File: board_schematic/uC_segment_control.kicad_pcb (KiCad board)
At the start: 2 copper layers, 69.9 x 41.9 mm, 14 parts, among them P1 CONN_02X05, P2 POWER_IN, U1 LF33

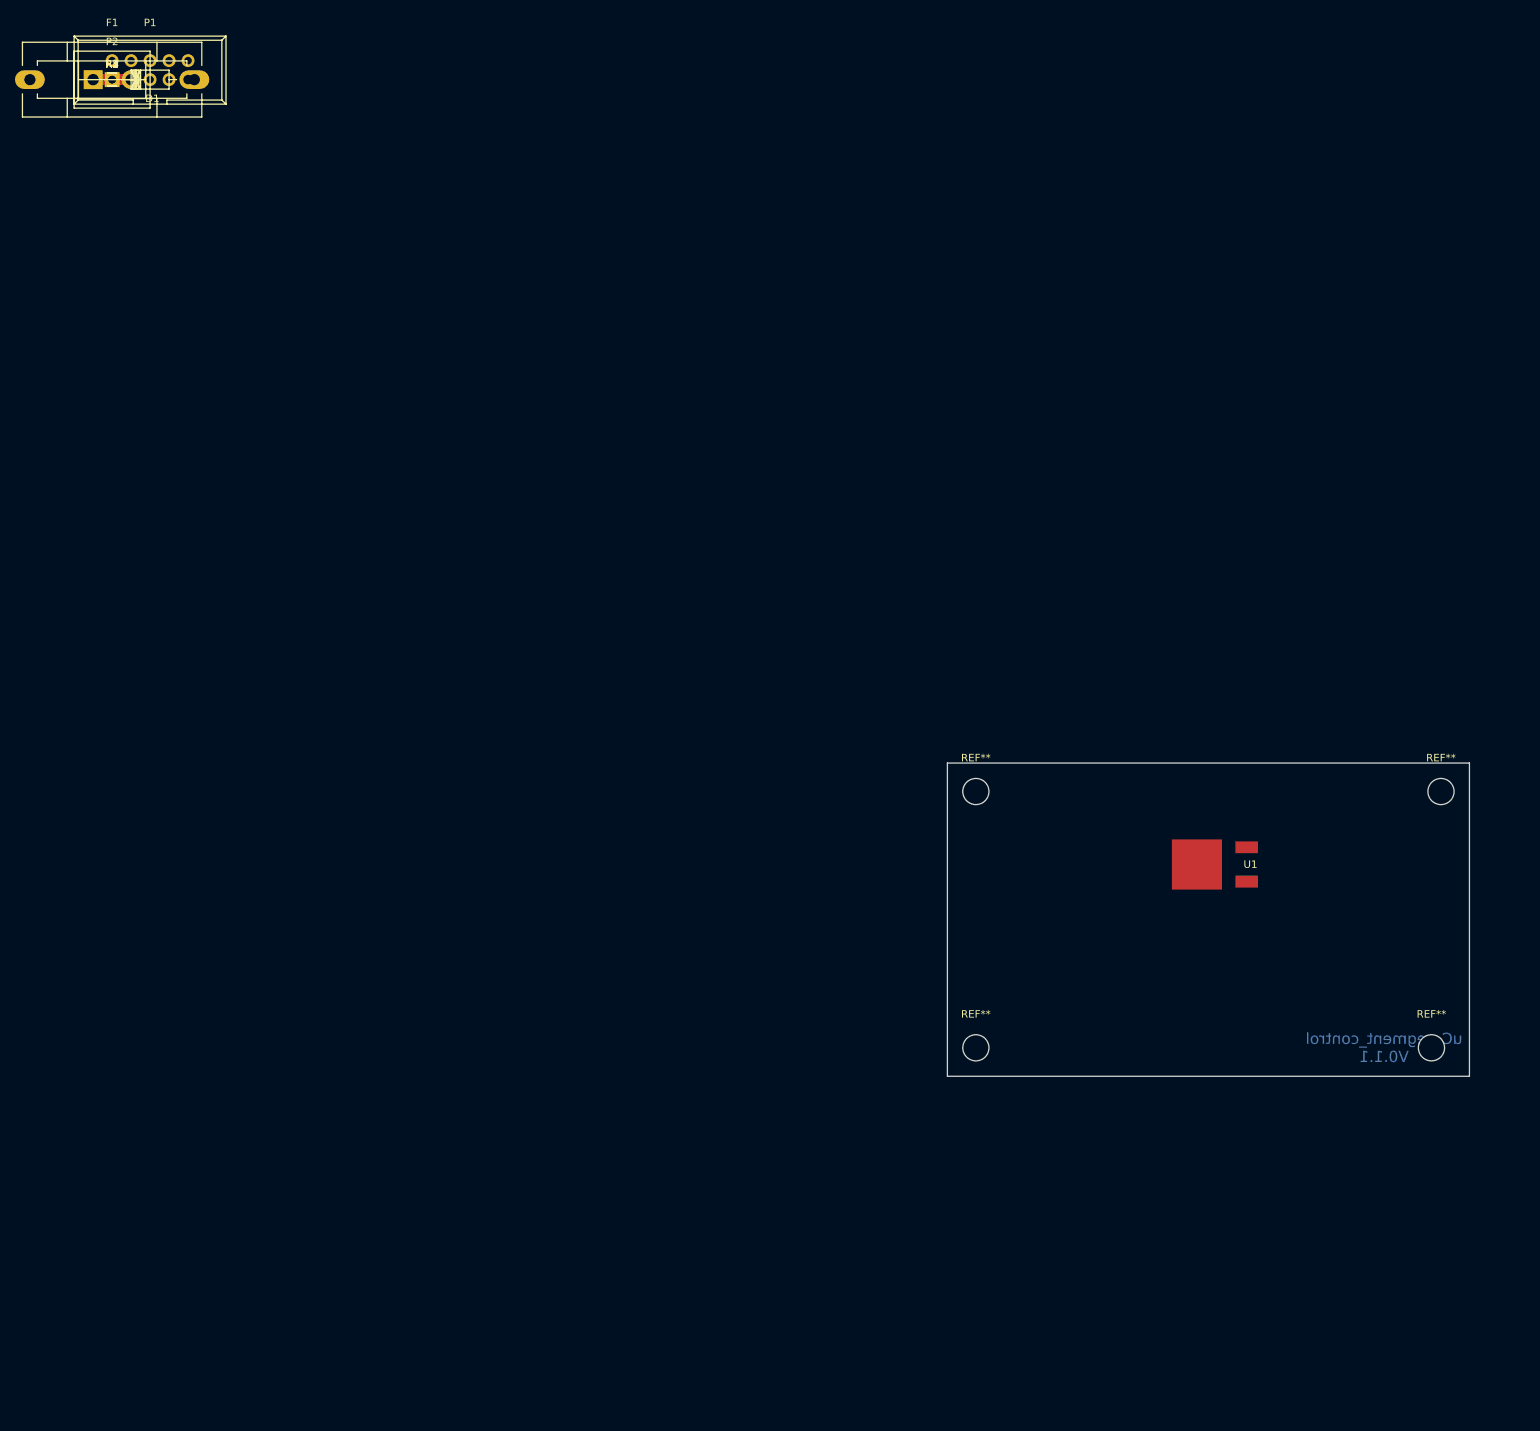
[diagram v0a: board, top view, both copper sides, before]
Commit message: V0.2.1: First schematic for BOM
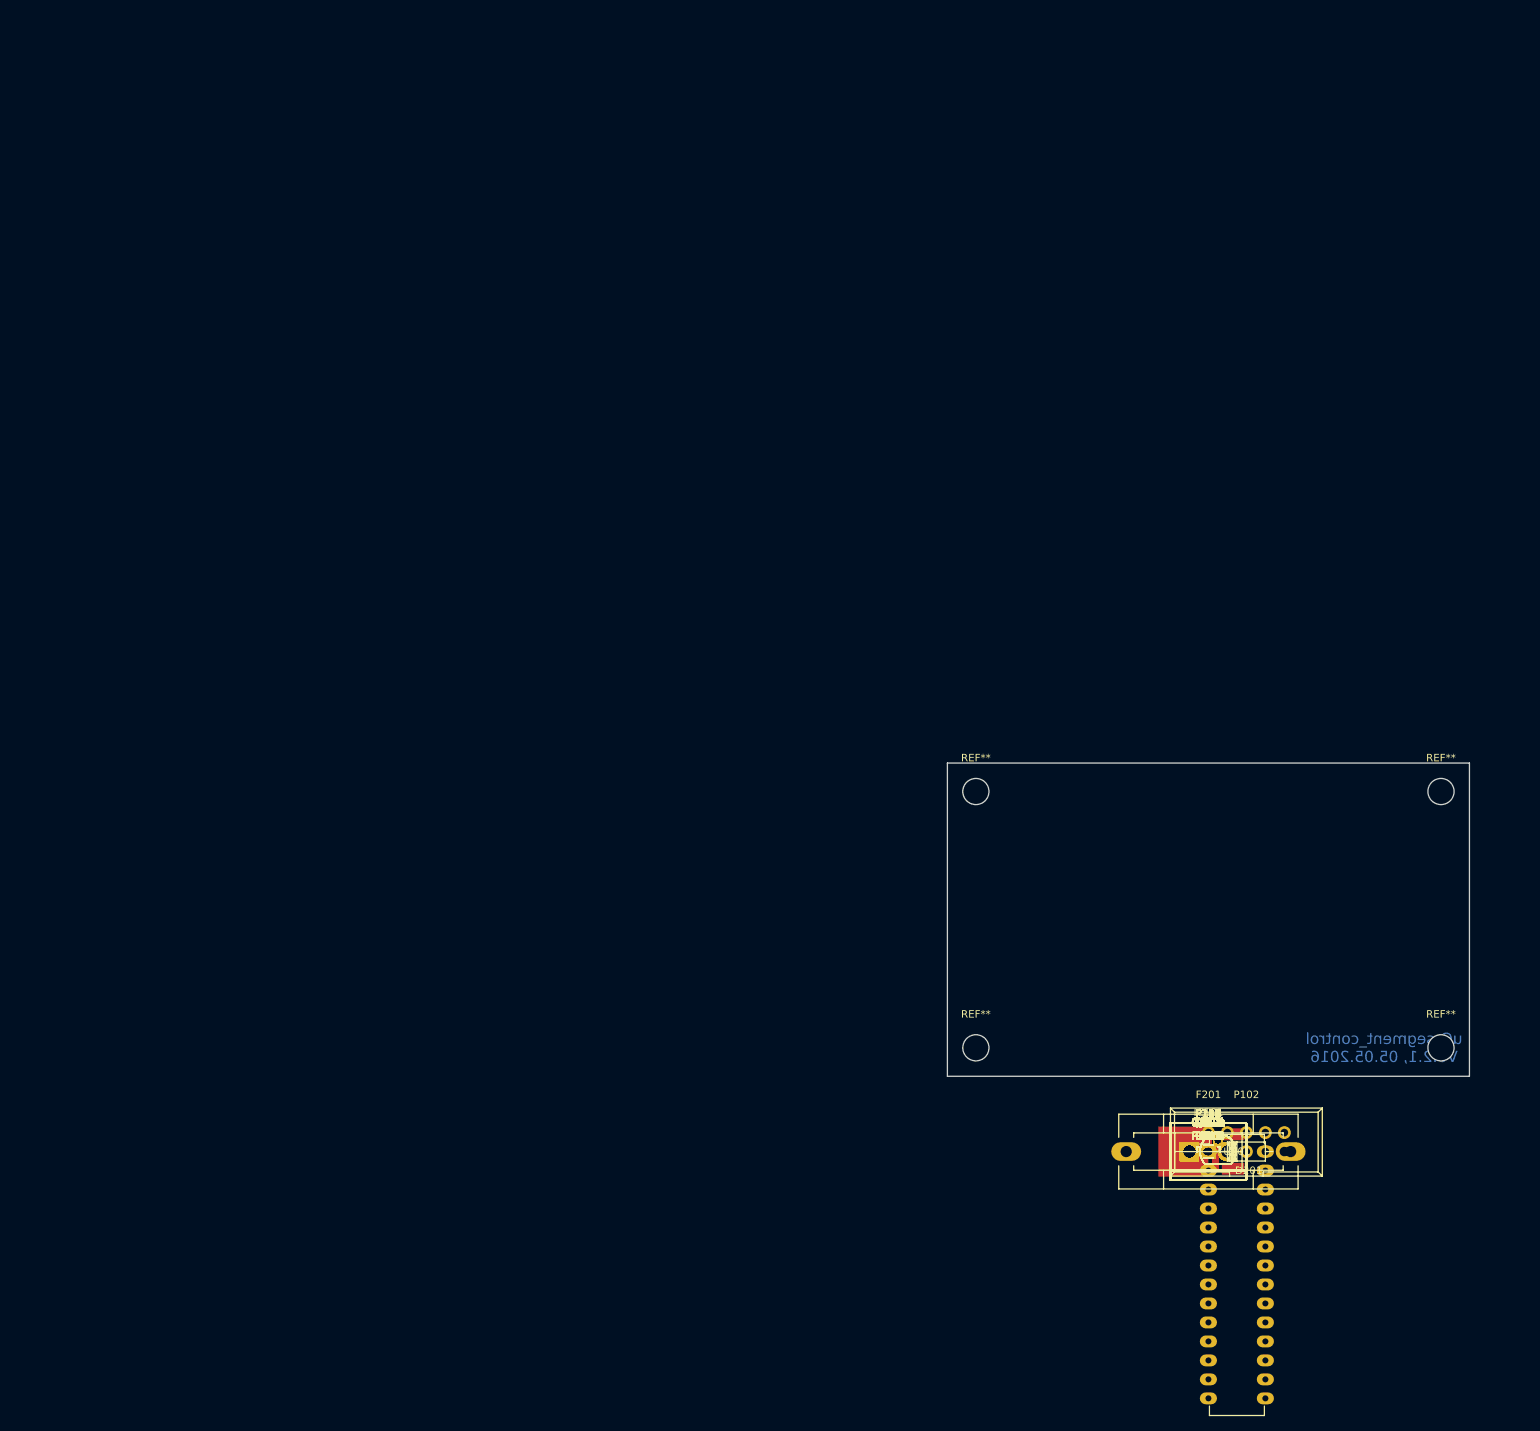
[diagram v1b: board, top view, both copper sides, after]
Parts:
- removed D1: ZD 15, Diodes_ThroughHole:Diode_DO-41_SOD81_Horizontal_RM10
- removed F1: 2.5A, Fuse_Holders_and_Fuses:Fuseholder5x20_horiz_SemiClosed_Casing10x25mm
- removed P1: CONN_02X05, Connect:IDC_Header_Straight_10pins
- removed P2: POWER_IN, Connect:bornier2
- removed R1, R2, R3, R4: 5k, Resistors_SMD:R_0805_HandSoldering
- removed R5: 10k, Resistors_SMD:R_0805_HandSoldering
- removed U1: LF33, project_footprints:D-PAK
- added C101: C, Capacitors_SMD:C_0805_HandSoldering, F.Cu at (146.7, 143.4)
- added C102: C_Small, Capacitors_SMD:C_0805_HandSoldering, F.Cu at (146.7, 143.4)
- added C201: 1uF (X7R-G0805 1,0/25), Capacitors_SMD:C_0805_HandSoldering, F.Cu at (146.7, 143.4)
- added C202: 10uF (X5R-G0805 10/16), Capacitors_SMD:C_0805_HandSoldering, F.Cu at (146.7, 143.4)
- added D201: ZD 15, Diodes_ThroughHole:Diode_DO-41_SOD81_Horizontal_RM10, F.Cu at (146.7, 143.4)
- added F201: F_Power, Fuse_Holders_and_Fuses:Fuseholder5x20_horiz_SemiClosed_Casing10x25mm, F.Cu at (146.7, 143.4)
- added IC101: ATMEGA88PA-P, Housings_DIP:DIP-28_W7.62mm_LongPads, F.Cu at (146.7, 143.4)
- added P101, P103, P104, P105, P106, P107, P108, P109, P110, P111, P112, P113, P114, P115, P116, P117, P118, P119, P120, P121, P122, P123, P124, P125, P126, P127, P128, P129, P130, P131, P132, P133, P134: CONN_01X02, Connect:bornier2, F.Cu at (146.7, 143.4)
- added P102: CONN_02X05, Connect:IDC_Header_Straight_10pins, F.Cu at (146.7, 143.4)
- added P201: CONN_01X02_P, Connect:bornier2, F.Cu at (146.7, 143.4)
- added Q1001, Q1101, Q1201, Q1301, Q1401, Q1501, Q1601, Q301, Q401, Q501, Q601, Q701, Q801, Q901: BC548, project_footprints:TO-92_Molded_0.6space_Oval, F.Cu at (146.7, 143.4)
- added Q1002, Q1102, Q1202, Q1302, Q1402, Q1502, Q1602, Q302, Q402, Q502, Q602, Q702, Q802, Q902: IRLML2244, TO_SOT_Packages_SMD:SOT-23_Handsoldering, F.Cu at (146.7, 143.4)
- added Q101, Q102, Q103, Q104, Q105, Q106: IRLML2502, TO_SOT_Packages_SMD:SOT-23_Handsoldering, F.Cu at (146.7, 143.4)
- added R1001, R1101, R1201, R1301, R1401, R1501, R1601, R301, R401, R501, R601, R701, R801, R901: 5k4, Resistors_SMD:R_0805_HandSoldering, F.Cu at (146.7, 143.4)
- added R1002, R1102, R1202, R1302, R1402, R1502, R1602, R302, R402, R502, R602, R702, R802, R902: 2k5, Resistors_SMD:R_0805_HandSoldering, F.Cu at (146.7, 143.4)
- added R1003, R1103, R1203, R1303, R1403, R1503, R1603, R303, R403, R503, R603, R703, R803, R903: 24k, Resistors_SMD:R_0805_HandSoldering, F.Cu at (146.7, 143.4)
- added R101, R102: 100, Resistors_SMD:R_0805_HandSoldering, F.Cu at (146.7, 143.4)
- added R103, R104, R105, R106: 5k, Resistors_SMD:R_0805_HandSoldering, F.Cu at (146.7, 143.4)
- added R107, R108, R109, R110, R111, R112: 250, Resistors_SMD:R_0805_HandSoldering, F.Cu at (146.7, 143.4)
- added R113: 10k, Resistors_SMD:R_0805_HandSoldering, F.Cu at (146.7, 143.4)
- added R114, R115, R116, R117, R118, R119: 3k3, Resistors_SMD:R_0805_HandSoldering, F.Cu at (146.7, 143.4)
- added U201: LF33, project_footprints:D-PAK, F.Cu at (146.7, 143.4)
- moved REF** 1.27 mm to (177.8, 129.5)
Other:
- net class Default: clearance 0.2 -> 0.6; trace_width 0.25 -> 1; via_dia 0.6 -> 1.5; via_drill 0.4 -> 0.8
- rule trace_clearance: 0.2 -> 0.6
- rule via_min_drill: 0.3 -> 0.8
- rule via_min_size: 0.4 -> 1.4
- board text added: "uC_segment_control V0.2.1, 05.05.2016"
- board text removed: "uC_segment_control V0.1.1"

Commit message: V0.3.1: First layout
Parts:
- removed P131, P132, P133, P134: CONN_01X02, Connect:bornier2
- removed the REF** at (115.6, 129.5)
- removed the REF** at (115.6, 95.2)
- removed the REF** at (177.8, 95.2)
- removed the REF** at (177.8, 129.5)
- added R120: 100, Resistors_SMD:R_0805_HandSoldering, B.Cu at (102.2, 126.8)
- added R121: 100, Resistors_SMD:R_0805_HandSoldering, B.Cu at (107.2, 126.8)
- added REF**: MountingHole_3mm, Mounting_Holes:MountingHole_3mm, F.Cu at (54.0, 140.0)
- added REF**: MountingHole_3mm, Mounting_Holes:MountingHole_3mm, F.Cu at (185.0, 140.0)
- added REF**: MountingHole_3mm, Mounting_Holes:MountingHole_3mm, F.Cu at (185.0, 54.0)
- added REF**: MountingHole_3mm, Mounting_Holes:MountingHole_3mm, F.Cu at (54.0, 54.0)
- C101: value C -> 100n; moved to B.Cu
- C102: value C_Small -> 100n; moved to B.Cu
- C201, C202, Q101, Q102, Q103, Q104, Q105, Q106, R116, R117, R118, U201: moved to B.Cu
- P101, P103, P104, P105, P106, P121, P122: value CONN_01X02 -> CONN_01X03; footprint Connect:bornier2 -> Connect:AK300-3
- P102: value CONN_02X05 -> CONN_01X03; footprint Connect:IDC_Header_Straight_10pins -> Connect:AK300-3
- P107, P108, P109, P110, P111, P112, P113, P114, P115, P116, P117, P118, P119, P120, P123, P124, P125, P126, P127, P129, P130, P201: footprint Connect:bornier2 -> Connect:AK300-2
- P128: value CONN_01X02 -> CONN_02X05; footprint Connect:bornier2 -> Connect:IDC_Header_Straight_10pins
- Q1001, Q1101, Q1201, Q1301, Q1401, Q1501, Q1601, Q301, Q401, Q501, Q601, Q701, Q801, Q901: value BC548 -> IRLML2244; footprint project_footprints:TO-92_Molded_0.6space_Oval -> TO_SOT_Packages_SMD:SOT-23_Handsoldering; moved to B.Cu
- Q1002, Q1102, Q1202, Q1302, Q1402, Q1502, Q1602, Q302, Q402, Q502, Q602, Q702, Q802, Q902: value IRLML2244 -> BC548; footprint TO_SOT_Packages_SMD:SOT-23_Handsoldering -> project_footprints:TO-92_Molded_0.6space_Oval
- R1001, R1101, R1201, R1301, R1401, R1501, R1601, R301, R401, R501, R601, R701, R801, R901: value 5k4 -> 27k; moved to B.Cu
- R1002, R1102, R1202, R1302, R1402, R1502, R1602, R302, R402, R502, R602, R702, R802, R902: value 2k5 -> 5k6; moved to B.Cu
- R1003, R1103, R1203, R1303, R1403, R1503, R1603, R303, R403, R503, R603, R703, R803, R903: value 24k -> 2k7; moved to B.Cu
- R101, R102: value 100 -> 270; moved to B.Cu
- R103: value 5k -> 270; moved to B.Cu
- R104, R105, R106: value 5k -> 3k3; moved to B.Cu
- R107: value 250 -> 10k; moved to B.Cu
- R108, R109, R110: value 250 -> 270; moved to B.Cu
- R111, R112: value 250 -> 5k; moved to B.Cu
- R113: value 10k -> 5k; moved to B.Cu
- R114, R115, R119: value 3k3 -> 5k; moved to B.Cu
- moved R302 119.1 mm to (55.2, 67.2)
- moved R303 116.7 mm to (55.2, 71.0)
- moved R402 115.3 mm to (60.2, 67.2)
- moved Q302 113.5 mm to (55.9, 75.2), turned to 90 degrees
- moved R403 112.8 mm to (60.2, 71.0)
- moved R502 111.6 mm to (65.2, 67.2)
- moved Q402 109.6 mm to (60.9, 75.2), turned to 90 degrees
- moved P119 109.3 mm to (55.5, 83.2)
- moved R503 109.1 mm to (65.2, 71.0)
- moved R602 108.0 mm to (70.2, 67.2)
- moved Q301 107.0 mm to (55.5, 87.5), turned to 180 degrees
- moved Q502 105.7 mm to (65.9, 75.2), turned to 90 degrees
- moved R603 105.4 mm to (70.2, 71.0)
- moved R301 105.4 mm to (55.5, 90.7)
- moved R702 104.5 mm to (75.2, 67.2)
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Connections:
- IC101 pad 21: (no net) -> Net-(IC101-Pad21)
- P101 pad 2: Net-(P101-Pad2) -> Net-(P101-Pad1)
- P102 pad 1: Net-(P102-Pad1) -> Net-(P101-Pad1)
- P102 pad 2: (no net) -> Net-(P101-Pad1)
- P102 pad 3: (no net) -> Net-(P101-Pad1)
- P103 pad 1: /p-mos_switch_S0_0.sch/S_OUT -> Net-(P103-Pad1)
- P103 pad 2: /p-mos_switch_S0_1.sch/S_OUT -> Net-(P103-Pad1)
- P104 pad 1: /p-mos_switch_S0_2.sch/S_OUT -> Net-(P103-Pad1)
- P104 pad 2: /p-mos_switch_S0_3.sch/S_OUT -> Net-(P103-Pad1)
- P105 pad 1: /p-mos_switch_S0_4.sch/S_OUT -> Net-(P105-Pad1)
- P105 pad 2: /p-mos_switch_S0_5.sch/S_OUT -> Net-(P105-Pad1)
- P106 pad 1: /p-mos_switch_S0_6.sch/S_OUT -> Net-(P105-Pad1)
- P106 pad 2: /p-mos_switch_S1_0.sch/S_OUT -> Net-(P105-Pad1)
- P107 pad 1: /p-mos_switch_S1_1.sch/S_OUT -> Net-(P101-Pad1)
- P107 pad 2: /p-mos_switch_S1_2.sch/S_OUT -> Net-(P101-Pad1)
- P108 pad 1: /p-mos_switch_S1_3.sch/S_OUT -> Net-(P101-Pad1)
- P108 pad 2: /p-mos_switch_S1_4.sch/S_OUT -> Net-(P101-Pad1)
- P109 pad 1: /p-mos_switch_S1_5.sch/S_OUT -> Net-(P103-Pad1)
- P109 pad 2: /p-mos_switch_S1_6.sch/S_OUT -> Net-(P103-Pad1)
- P110 pad 1: +12.0V -> Net-(P103-Pad1)
- P110 pad 2: +12.0V -> Net-(P103-Pad1)
- P111 pad 1: Net-(P111-Pad1) -> Net-(P105-Pad1)
- P111 pad 2: Net-(P111-Pad1) -> Net-(P105-Pad1)
- P112 pad 1: Net-(P111-Pad1) -> Net-(P105-Pad1)
- P112 pad 2: Net-(P111-Pad1) -> Net-(P105-Pad1)
- P113 pad 1: Net-(P111-Pad1) -> Net-(P101-Pad1)
- P113 pad 2: Net-(P111-Pad1) -> Net-(P101-Pad1)
- P114 pad 1: Net-(P111-Pad1) -> Net-(P101-Pad1)
- P114 pad 2: Net-(P111-Pad1) -> Net-(P101-Pad1)
- P115 pad 1: Net-(P115-Pad1) -> Net-(P103-Pad1)
- P115 pad 2: Net-(P115-Pad1) -> Net-(P103-Pad1)
- P116 pad 1: Net-(P111-Pad1) -> Net-(P103-Pad1)
- P116 pad 2: Net-(P111-Pad1) -> Net-(P103-Pad1)
- P117 pad 1: Net-(P111-Pad1) -> Net-(P105-Pad1)
- P117 pad 2: Net-(P111-Pad1) -> Net-(P105-Pad1)
- P118 pad 1: Net-(P111-Pad1) -> Net-(P105-Pad1)
- P118 pad 2: Net-(P111-Pad1) -> Net-(P105-Pad1)
- P119 pad 1: Net-(P119-Pad1) -> /p-mos_switch_S0_0.sch/S_OUT
- P119 pad 2: Net-(P119-Pad1) -> /p-mos_switch_S0_1.sch/S_OUT
- P120 pad 1: Net-(P119-Pad1) -> /p-mos_switch_S0_2.sch/S_OUT
- P120 pad 2: Net-(P119-Pad1) -> /p-mos_switch_S0_3.sch/S_OUT
- P121 pad 1: Net-(P119-Pad1) -> /p-mos_switch_S0_4.sch/S_OUT
- P121 pad 2: Net-(P119-Pad1) -> /p-mos_switch_S0_5.sch/S_OUT
- P122 pad 1: Net-(P119-Pad1) -> /p-mos_switch_S1_0.sch/S_OUT
- P122 pad 2: Net-(P119-Pad1) -> /p-mos_switch_S1_1.sch/S_OUT
- P123 pad 1: Net-(P123-Pad1) -> /p-mos_switch_S1_3.sch/S_OUT
- P123 pad 2: Net-(P123-Pad1) -> /p-mos_switch_S1_4.sch/S_OUT
- P124 pad 1: Net-(P119-Pad1) -> /p-mos_switch_S1_5.sch/S_OUT
- P124 pad 2: Net-(P119-Pad1) -> /p-mos_switch_S1_6.sch/S_OUT
- P125 pad 1: Net-(P119-Pad1) -> Net-(P125-Pad1)
- P125 pad 2: Net-(P119-Pad1) -> Net-(P125-Pad1)
- P126 pad 1: Net-(P119-Pad1) -> Net-(P126-Pad1)
- P126 pad 2: Net-(P119-Pad1) -> Net-(P126-Pad1)
- P128 pad 1: Net-(P127-Pad1) -> Net-(P128-Pad1)
- P128 pad 2: Net-(P127-Pad1) -> Net-(P128-Pad2)
- P129 pad 1: Net-(P127-Pad1) -> +12.0V
- P129 pad 2: Net-(P127-Pad1) -> +12.0V
- P130 pad 1: Net-(P127-Pad1) -> Net-(P130-Pad1)
- P130 pad 2: Net-(P127-Pad1) -> Net-(P130-Pad2)
- Q1001 pad 2: Net-(Q1001-Pad2) -> +12.0V
- Q1001 pad 3: GND -> /p-mos_switch_S1_0.sch/S_OUT
- Q1002 pad 2: +12.0V -> Net-(Q1002-Pad2)
- Q1002 pad 3: /p-mos_switch_S1_0.sch/S_OUT -> GND
- Q101 pad 3: Net-(P111-Pad1) -> Net-(P101-Pad1)
- Q102 pad 1: /G1_R -> /G0_G
- Q102 pad 3: Net-(P115-Pad1) -> Net-(P103-Pad1)
- Q103 pad 1: /G0_G -> /G0_B
- Q103 pad 3: Net-(P119-Pad1) -> Net-(P105-Pad1)
- Q104 pad 1: /G1_G -> /G1_R
- Q104 pad 3: Net-(P123-Pad1) -> Net-(P125-Pad1)
- Q105 pad 1: /G0_B -> /G1_G
- Q105 pad 3: Net-(P127-Pad1) -> Net-(P126-Pad1)
- Q106 pad 3: Net-(P131-Pad1) -> Net-(P127-Pad1)
- Q1101 pad 2: Net-(Q1101-Pad2) -> +12.0V
- Q1101 pad 3: GND -> /p-mos_switch_S1_1.sch/S_OUT
- Q1102 pad 2: +12.0V -> Net-(Q1102-Pad2)
- Q1102 pad 3: /p-mos_switch_S1_1.sch/S_OUT -> GND
- Q1201 pad 2: Net-(Q1201-Pad2) -> +12.0V
- Q1201 pad 3: GND -> /p-mos_switch_S1_2.sch/S_OUT
- Q1202 pad 2: +12.0V -> Net-(Q1202-Pad2)
- Q1202 pad 3: /p-mos_switch_S1_2.sch/S_OUT -> GND
- Q1301 pad 2: Net-(Q1301-Pad2) -> +12.0V
- Q1301 pad 3: GND -> /p-mos_switch_S1_3.sch/S_OUT
- Q1302 pad 2: +12.0V -> Net-(Q1302-Pad2)
- Q1302 pad 3: /p-mos_switch_S1_3.sch/S_OUT -> GND
- Q1401 pad 2: Net-(Q1401-Pad2) -> +12.0V
- Q1401 pad 3: GND -> /p-mos_switch_S1_4.sch/S_OUT
- Q1402 pad 2: +12.0V -> Net-(Q1402-Pad2)
- Q1402 pad 3: /p-mos_switch_S1_4.sch/S_OUT -> GND
- Q1501 pad 2: Net-(Q1501-Pad2) -> +12.0V
- Q1501 pad 3: GND -> /p-mos_switch_S1_5.sch/S_OUT
- Q1502 pad 2: +12.0V -> Net-(Q1502-Pad2)
- Q1502 pad 3: /p-mos_switch_S1_5.sch/S_OUT -> GND
- Q1601 pad 2: Net-(Q1601-Pad2) -> +12.0V
- Q1601 pad 3: GND -> /p-mos_switch_S1_6.sch/S_OUT
- Q1602 pad 2: +12.0V -> Net-(Q1602-Pad2)
- Q1602 pad 3: /p-mos_switch_S1_6.sch/S_OUT -> GND
- Q301 pad 2: Net-(Q301-Pad2) -> +12.0V
- Q301 pad 3: GND -> /p-mos_switch_S0_0.sch/S_OUT
- Q302 pad 2: +12.0V -> Net-(Q302-Pad2)
- Q302 pad 3: /p-mos_switch_S0_0.sch/S_OUT -> GND
- Q401 pad 2: Net-(Q401-Pad2) -> +12.0V
- Q401 pad 3: GND -> /p-mos_switch_S0_1.sch/S_OUT
- Q402 pad 2: +12.0V -> Net-(Q402-Pad2)
- Q402 pad 3: /p-mos_switch_S0_1.sch/S_OUT -> GND
- Q501 pad 2: Net-(Q501-Pad2) -> +12.0V
- Q501 pad 3: GND -> /p-mos_switch_S0_2.sch/S_OUT
- Q502 pad 2: +12.0V -> Net-(Q502-Pad2)
- Q502 pad 3: /p-mos_switch_S0_2.sch/S_OUT -> GND
- Q601 pad 2: Net-(Q601-Pad2) -> +12.0V
- Q601 pad 3: GND -> /p-mos_switch_S0_3.sch/S_OUT
- Q602 pad 2: +12.0V -> Net-(Q602-Pad2)
- Q602 pad 3: /p-mos_switch_S0_3.sch/S_OUT -> GND
- Q701 pad 2: Net-(Q701-Pad2) -> +12.0V
- Q701 pad 3: GND -> /p-mos_switch_S0_4.sch/S_OUT
- Q702 pad 2: +12.0V -> Net-(Q702-Pad2)
- Q702 pad 3: /p-mos_switch_S0_4.sch/S_OUT -> GND
- Q801 pad 2: Net-(Q801-Pad2) -> +12.0V
- Q801 pad 3: GND -> /p-mos_switch_S0_5.sch/S_OUT
- Q802 pad 2: +12.0V -> Net-(Q802-Pad2)
- Q802 pad 3: /p-mos_switch_S0_5.sch/S_OUT -> GND
- Q901 pad 2: Net-(Q901-Pad2) -> +12.0V
- Q901 pad 3: GND -> /p-mos_switch_S0_6.sch/S_OUT
- Q902 pad 2: +12.0V -> Net-(Q902-Pad2)
- Q902 pad 3: /p-mos_switch_S0_6.sch/S_OUT -> GND
- R1001 pad 1: Net-(Q1001-Pad2) -> +12.0V
- R1001 pad 2: /p-mos_switch_S1_0.sch/S_IN -> Net-(Q1001-Pad1)
- R1002 pad 1: Net-(Q1001-Pad2) -> Net-(Q1002-Pad2)
- R1002 pad 2: GND -> /p-mos_switch_S1_0.sch/S_IN
- R1003 pad 1: +12.0V -> Net-(Q1002-Pad2)
- R1003 pad 2: Net-(Q1001-Pad1) -> GND
- R101 pad 1: Net-(P101-Pad1) -> /G0_G
- R101 pad 2: /SDA -> Net-(IC101-Pad15)
- R102 pad 1: Net-(P101-Pad2) -> /G1_G
- R102 pad 2: /SCL -> Net-(IC101-Pad16)
- R103 pad 1: /MOSI -> /G0_B
- R103 pad 2: Net-(P102-Pad1) -> /MOSI
- R104 pad 1: /RESET -> /G0_R
- R104 pad 2: Net-(P102-Pad5) -> GND
- R105 pad 1: /p-mos_switch_S0_2.sch/S_IN -> /G0_G
- R105 pad 2: Net-(P102-Pad7) -> GND
- R106 pad 1: /p-mos_switch_S0_1.sch/S_IN -> /G0_B
- R106 pad 2: Net-(P102-Pad9) -> GND
- R107 pad 1: /G0_G -> /RESET
- R107 pad 2: Net-(IC101-Pad15) -> +3.3V
- R108 pad 1: /G1_G -> /G1_B
- R108 pad 2: Net-(IC101-Pad16) -> Net-(IC101-Pad5)
- R109 pad 1: /G0_B -> /G1_R
- R109 pad 2: /MOSI -> Net-(IC101-Pad11)
- R110 pad 1: /G1_B -> /G0_R
- R110 pad 2: Net-(IC101-Pad5) -> Net-(IC101-Pad12)
- R1101 pad 1: Net-(Q1101-Pad2) -> +12.0V
- R1101 pad 2: /p-mos_switch_S1_1.sch/S_IN -> Net-(Q1101-Pad1)
- R1102 pad 1: Net-(Q1101-Pad2) -> Net-(Q1102-Pad2)
- R1102 pad 2: GND -> /p-mos_switch_S1_1.sch/S_IN
- R1103 pad 1: +12.0V -> Net-(Q1102-Pad2)
- R1103 pad 2: Net-(Q1101-Pad1) -> GND
- R111 pad 1: /G1_R -> /MOSI
- R111 pad 2: Net-(IC101-Pad11) -> Net-(P128-Pad1)
- R112 pad 1: /G0_R -> Net-(P128-Pad4)
- R112 pad 2: Net-(IC101-Pad12) -> /p-mos_switch_S1_2.sch/S_IN
- R113 pad 2: +3.3V -> Net-(P128-Pad5)
- R114 pad 1: /G0_R -> Net-(P128-Pad6)
- R114 pad 2: GND -> /p-mos_switch_S1_3.sch/S_IN
- R115 pad 1: /G1_R -> /p-mos_switch_S0_2.sch/S_IN
- R115 pad 2: GND -> Net-(P128-Pad7)
- R116 pad 1: /G0_G -> /G1_R
- R118 pad 1: /G0_B -> /G1_B
- R119 pad 1: /G1_B -> /p-mos_switch_S0_1.sch/S_IN
- R119 pad 2: GND -> Net-(P128-Pad9)
- R1201 pad 1: Net-(Q1201-Pad2) -> +12.0V
- R1201 pad 2: /p-mos_switch_S1_2.sch/S_IN -> Net-(Q1201-Pad1)
- R1202 pad 1: Net-(Q1201-Pad2) -> Net-(Q1202-Pad2)
- R1202 pad 2: GND -> /p-mos_switch_S1_2.sch/S_IN
- R1203 pad 1: +12.0V -> Net-(Q1202-Pad2)
- R1203 pad 2: Net-(Q1201-Pad1) -> GND
- R1301 pad 1: Net-(Q1301-Pad2) -> +12.0V
- R1301 pad 2: /p-mos_switch_S1_3.sch/S_IN -> Net-(Q1301-Pad1)
- R1302 pad 1: Net-(Q1301-Pad2) -> Net-(Q1302-Pad2)
- R1302 pad 2: GND -> /p-mos_switch_S1_3.sch/S_IN
- R1303 pad 1: +12.0V -> Net-(Q1302-Pad2)
- R1303 pad 2: Net-(Q1301-Pad1) -> GND
- R1401 pad 1: Net-(Q1401-Pad2) -> +12.0V
- R1401 pad 2: /p-mos_switch_S1_4.sch/S_IN -> Net-(Q1401-Pad1)
- R1402 pad 1: Net-(Q1401-Pad2) -> Net-(Q1402-Pad2)
- R1402 pad 2: GND -> /p-mos_switch_S1_4.sch/S_IN
- R1403 pad 1: +12.0V -> Net-(Q1402-Pad2)
- R1403 pad 2: Net-(Q1401-Pad1) -> GND
- R1501 pad 1: Net-(Q1501-Pad2) -> +12.0V
- R1501 pad 2: /p-mos_switch_S1_5.sch/S_IN -> Net-(Q1501-Pad1)
- R1502 pad 1: Net-(Q1501-Pad2) -> Net-(Q1502-Pad2)
- R1502 pad 2: GND -> /p-mos_switch_S1_5.sch/S_IN
- R1503 pad 1: +12.0V -> Net-(Q1502-Pad2)
- R1503 pad 2: Net-(Q1501-Pad1) -> GND
- R1601 pad 1: Net-(Q1601-Pad2) -> +12.0V
- R1601 pad 2: /p-mos_switch_S1_6.sch/S_IN -> Net-(Q1601-Pad1)
- R1602 pad 1: Net-(Q1601-Pad2) -> Net-(Q1602-Pad2)
- R1602 pad 2: GND -> /p-mos_switch_S1_6.sch/S_IN
- R1603 pad 1: +12.0V -> Net-(Q1602-Pad2)
- R1603 pad 2: Net-(Q1601-Pad1) -> GND
- R301 pad 1: Net-(Q301-Pad2) -> +12.0V
- R301 pad 2: /p-mos_switch_S0_0.sch/S_IN -> Net-(Q301-Pad1)
- R302 pad 1: Net-(Q301-Pad2) -> Net-(Q302-Pad2)
- R302 pad 2: GND -> /p-mos_switch_S0_0.sch/S_IN
- R303 pad 1: +12.0V -> Net-(Q302-Pad2)
- R303 pad 2: Net-(Q301-Pad1) -> GND
- R401 pad 1: Net-(Q401-Pad2) -> +12.0V
- R401 pad 2: /p-mos_switch_S0_1.sch/S_IN -> Net-(Q401-Pad1)
- R402 pad 1: Net-(Q401-Pad2) -> Net-(Q402-Pad2)
- R402 pad 2: GND -> /p-mos_switch_S0_1.sch/S_IN
- R403 pad 1: +12.0V -> Net-(Q402-Pad2)
- R403 pad 2: Net-(Q401-Pad1) -> GND
- R501 pad 1: Net-(Q501-Pad2) -> +12.0V
- R501 pad 2: /p-mos_switch_S0_2.sch/S_IN -> Net-(Q501-Pad1)
- R502 pad 1: Net-(Q501-Pad2) -> Net-(Q502-Pad2)
- R502 pad 2: GND -> /p-mos_switch_S0_2.sch/S_IN
- R503 pad 1: +12.0V -> Net-(Q502-Pad2)
- R503 pad 2: Net-(Q501-Pad1) -> GND
- R601 pad 1: Net-(Q601-Pad2) -> +12.0V
- R601 pad 2: /p-mos_switch_S0_3.sch/S_IN -> Net-(Q601-Pad1)
- R602 pad 1: Net-(Q601-Pad2) -> Net-(Q602-Pad2)
- R602 pad 2: GND -> /p-mos_switch_S0_3.sch/S_IN
- R603 pad 1: +12.0V -> Net-(Q602-Pad2)
- R603 pad 2: Net-(Q601-Pad1) -> GND
- R701 pad 1: Net-(Q701-Pad2) -> +12.0V
- R701 pad 2: /p-mos_switch_S0_4.sch/S_IN -> Net-(Q701-Pad1)
- R702 pad 1: Net-(Q701-Pad2) -> Net-(Q702-Pad2)
- R702 pad 2: GND -> /p-mos_switch_S0_4.sch/S_IN
- R703 pad 1: +12.0V -> Net-(Q702-Pad2)
- R703 pad 2: Net-(Q701-Pad1) -> GND
- R801 pad 1: Net-(Q801-Pad2) -> +12.0V
- R801 pad 2: /p-mos_switch_S0_5.sch/S_IN -> Net-(Q801-Pad1)
- R802 pad 1: Net-(Q801-Pad2) -> Net-(Q802-Pad2)
- R802 pad 2: GND -> /p-mos_switch_S0_5.sch/S_IN
- R803 pad 1: +12.0V -> Net-(Q802-Pad2)
- R803 pad 2: Net-(Q801-Pad1) -> GND
- R901 pad 1: Net-(Q901-Pad2) -> +12.0V
- R901 pad 2: /p-mos_switch_S0_6.sch/S_IN -> Net-(Q901-Pad1)
- R902 pad 1: Net-(Q901-Pad2) -> Net-(Q902-Pad2)
- R902 pad 2: GND -> /p-mos_switch_S0_6.sch/S_IN
- R903 pad 1: +12.0V -> Net-(Q902-Pad2)
- R903 pad 2: Net-(Q901-Pad1) -> GND
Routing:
- net GND: track 0.00 -> 727.4 mm, vias 0 -> 29
- net Net-(P101-Pad1): track 0.00 -> 260.5 mm
- net +12.0V: track 0.00 -> 246.8 mm, vias 0 -> 3
- net Net-(P103-Pad1): track 0.00 -> 227.5 mm, vias 0 -> 2
- net Net-(P105-Pad1): track 0.00 -> 210.5 mm, vias 0 -> 2
- net /p-mos_switch_S0_3.sch/S_IN: track 0.00 -> 115.1 mm, vias 0 -> 2
- net /p-mos_switch_S1_3.sch/S_IN: track 0.00 -> 115.0 mm, vias 0 -> 4
- net /p-mos_switch_S1_0.sch/S_IN: track 0.00 -> 111.6 mm
- net /p-mos_switch_S1_6.sch/S_IN: track 0.00 -> 106.4 mm, vias 0 -> 2
- net /p-mos_switch_S0_0.sch/S_IN: track 0.00 -> 105.1 mm
- net /p-mos_switch_S0_4.sch/S_IN: track 0.00 -> 104.7 mm, vias 0 -> 2
- net /p-mos_switch_S1_5.sch/S_IN: track 0.00 -> 101.4 mm, vias 0 -> 2
- net /p-mos_switch_S1_1.sch/S_IN: track 0.00 -> 101.0 mm
- net Net-(IC101-Pad16): track 0.00 -> 90.8 mm, vias 0 -> 2
- net /p-mos_switch_S1_2.sch/S_IN: track 0.00 -> 89.2 mm, vias 0 -> 2
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- added copper zone on B.Cu, net GND
- added copper zone on F.Cu, net GND
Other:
- board size 69.9 x 41.9 mm -> 139 x 94 mm
- net class Default: via_dia 1.5 -> 1.8
- rule pad_to_mask_clearance: 0.2 -> 0
- rule trace_min: 0.2 -> 0.5
- rule via_min_drill: 0.8 -> 0.6
- rule via_min_size: 1.4 -> 1.2
- board text added: "BGR S 0_6"
- board text added: "Each transistors (THT) above clamps to make sure that cables do not bend transistors"
- board text added: "Power tracks (12V) should be 1mm (track width) because of the warming. Other tracks are also 1mm for easy milling."
- board text added: "Power-IN in the middle of the board for short tracks on board (voltage drop on board is higher than over cable)"
- board text added: "RGB S 1_6"
- board text added: "The front layer can be replaced by copper wires. (No via is under a flat part, no via between clamps to avoid short cut with LED-wires, always a via next to every THT-pad for wires and bottom-soldering,...)"
- board text added: "uC_segment_control 2016-05-12 V0.3.1"
- board text removed: "uC_segment_control V0.2.1, 05.05.2016"
